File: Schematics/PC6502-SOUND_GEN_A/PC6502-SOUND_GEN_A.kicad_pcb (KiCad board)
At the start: 4 copper layers, 100 x 100 mm, 71 parts, among them IC1 AS7C164A-15PCN, IC2 AS7C164A-15PCN, IC3 AS7C164A-15PCN, IC4 AS7C164A-15PCN, IC5 AS7C164A-15PCN, IC6 AS7C164A-15PCN, J1 BUS, J2 NCO_OUT, J3 SND0/SND1, J5 Conn_02x05_Odd_Even, U1 74LS283, U10 74HCT574, U11 74HCT574, U12 74HC245, U13 74LS283, U14 74LS283, U15 74HCT574, U16 74HCT138, U2 74HC245, U3 74LS283, U4 ATF1502AS, U5 74HC245, U6 74AHCT244, U7 74HC14, U8 74LS283, U9 74LS283, X1 CXO_DIP8

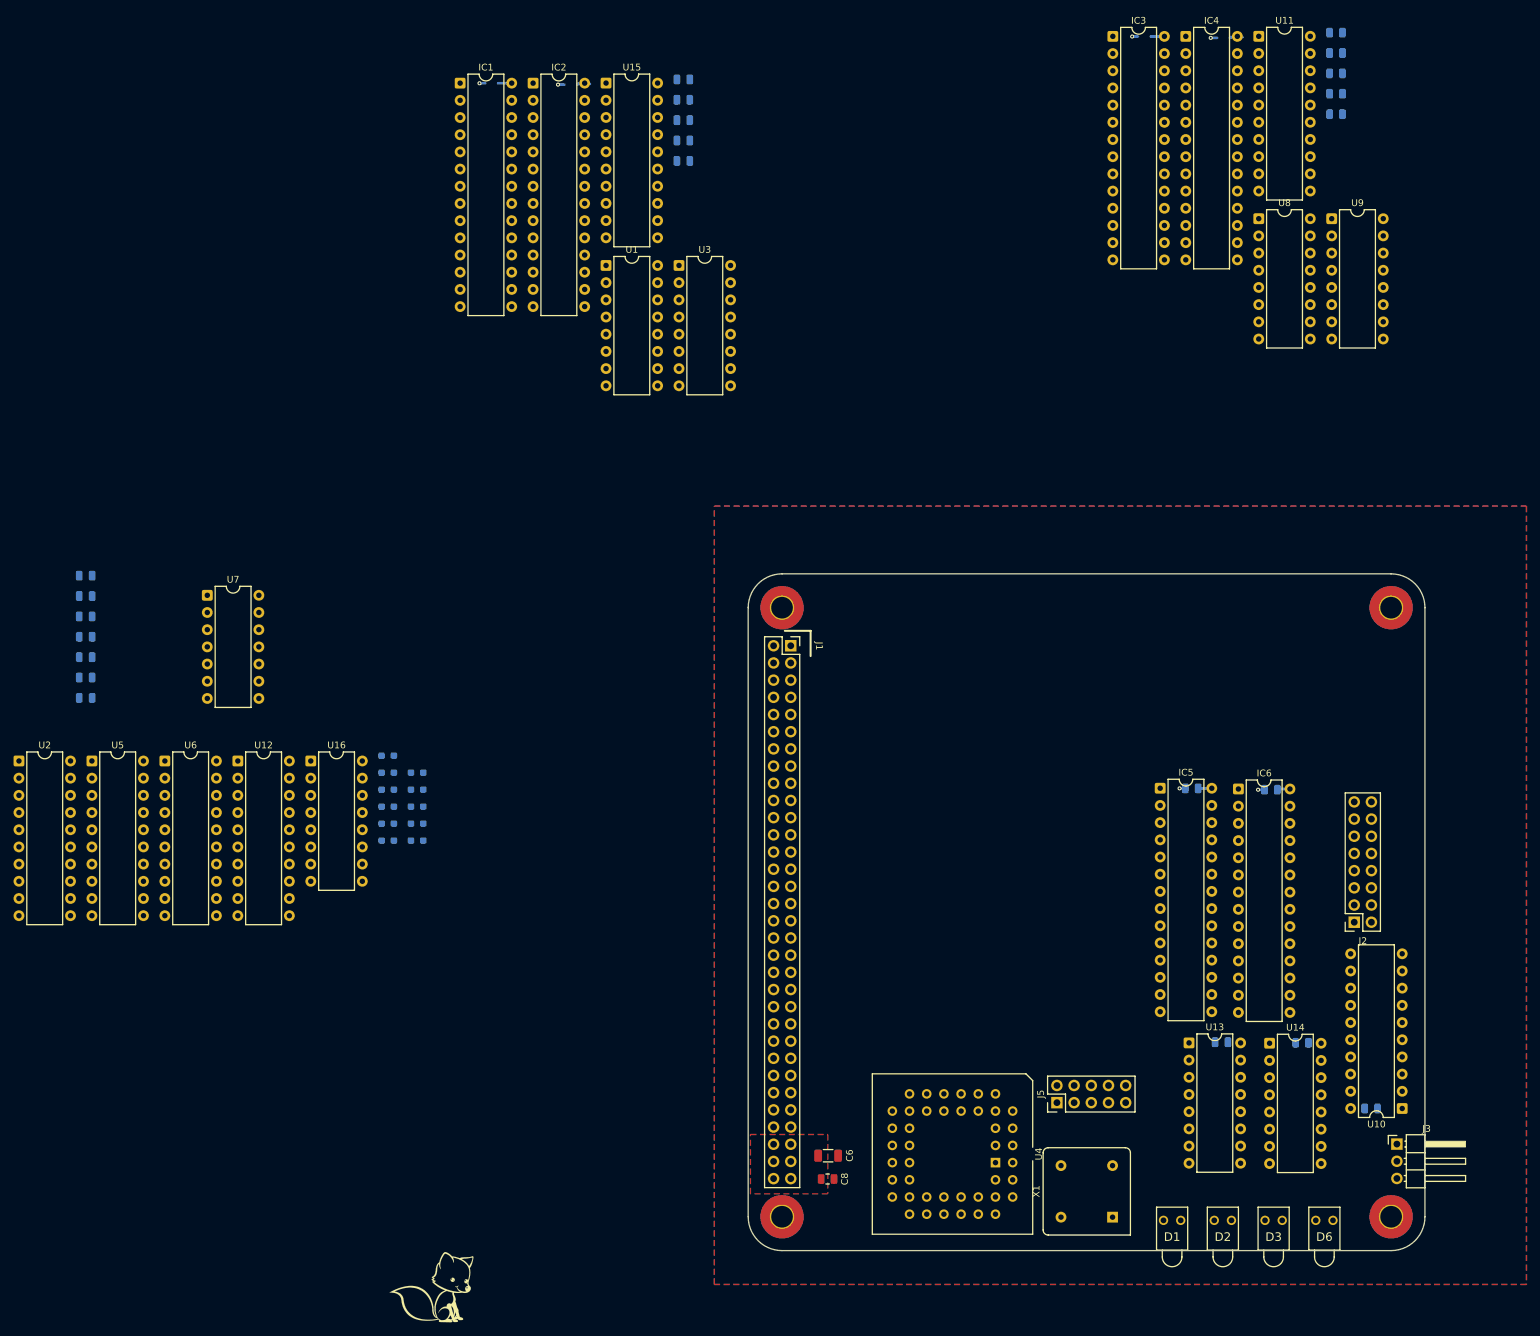
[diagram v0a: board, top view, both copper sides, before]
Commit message: Created V1.1 Schematic and PCB
A LOT of changes from v1.00;
removed clock stretcher (will now live in the CPLD)
moved the USB interface direct to the PCB
changed power pins
Added extra capacitance
Used Grant Searle's OSI basic and memory map to bring up the board
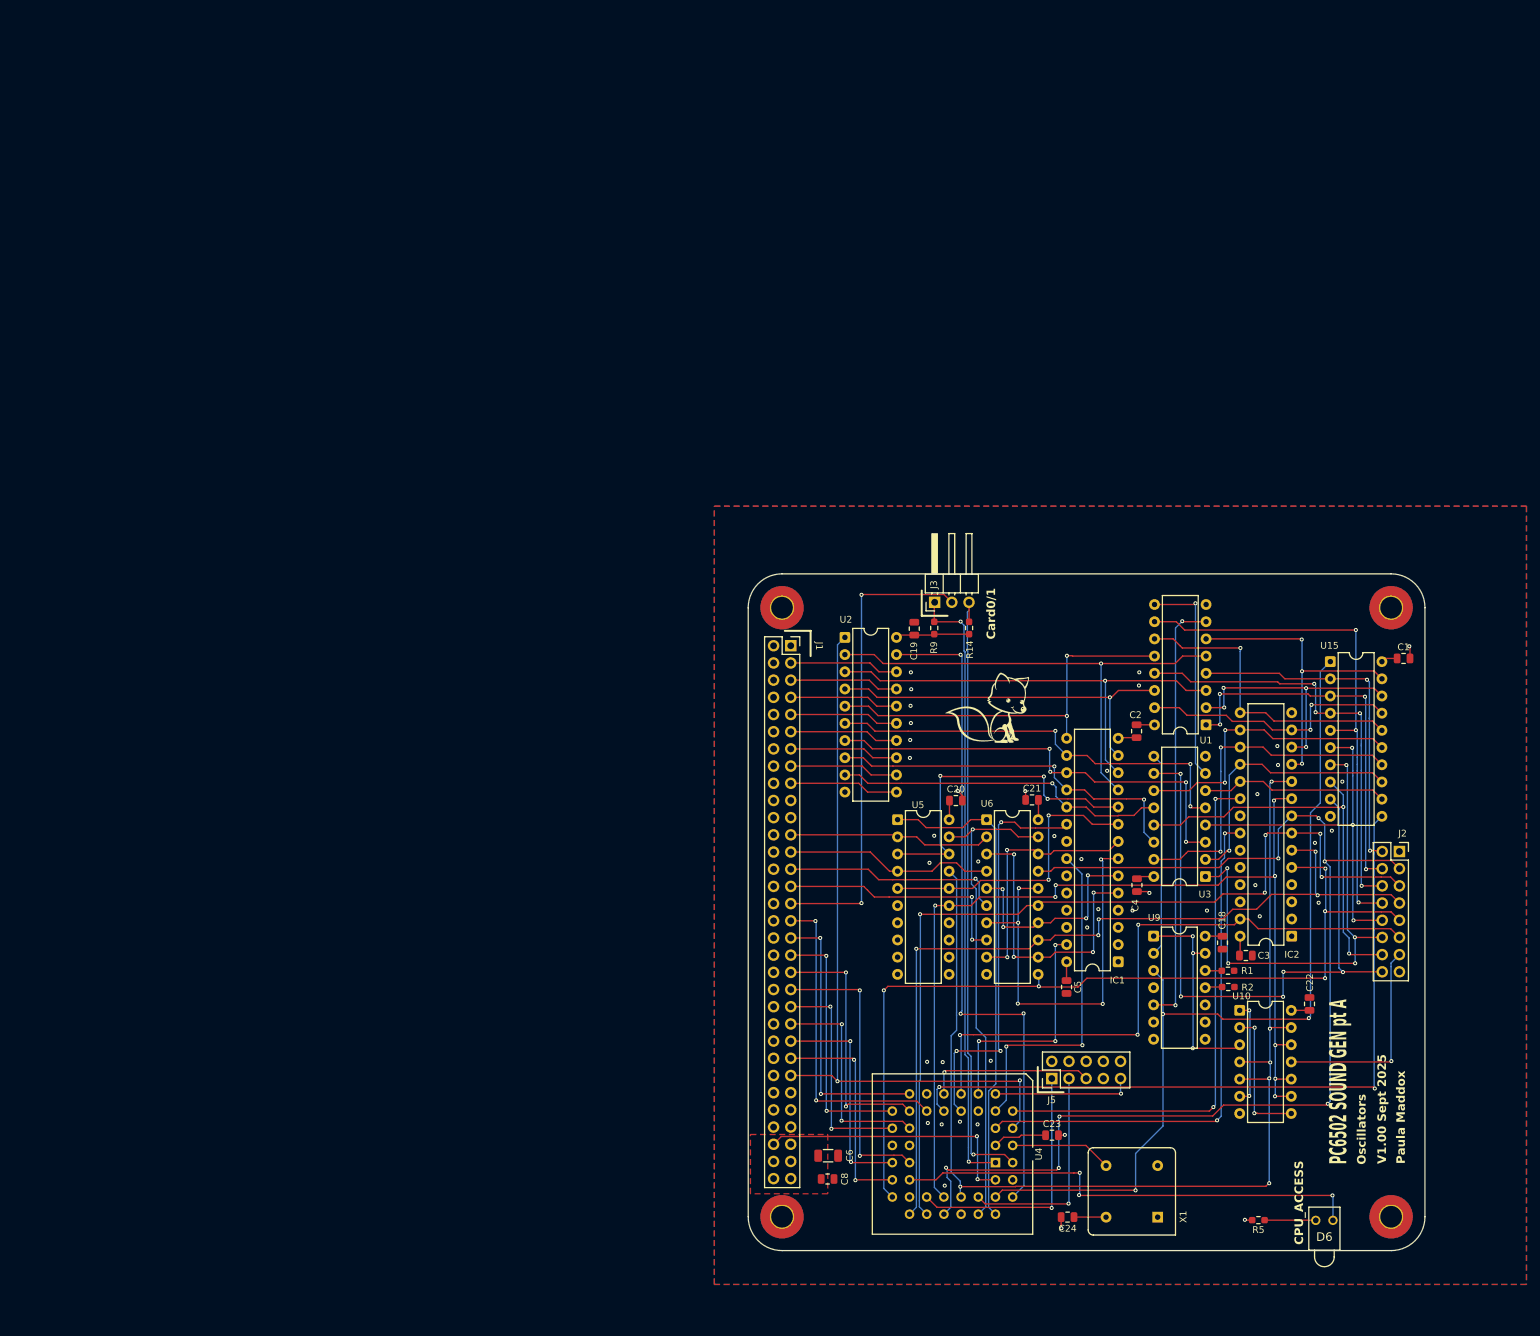
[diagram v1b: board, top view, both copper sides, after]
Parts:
- removed C10, C11, C12, C13, C14, C15, C16, C17, C7, C9: 100nF, Capacitor_SMD:C_0805_2012Metric
- removed D1, D2, D3: LED, LTL-4221NHBP:LTL4221NHBP
- removed IC3, IC4, IC5, IC6: AS7C164A-15PCN, Package_DIP:DIP-28_W7.62mm
- removed R10, R3, R4: 10K, Resistor_SMD:R_0603_1608Metric_Pad0.98x0.95mm_HandSolder
- removed R6, R7, R8: 470R, Resistor_SMD:R_0603_1608Metric_Pad0.98x0.95mm_HandSolder
- removed U11: 74HCT574, Package_DIP:DIP-20_W7.62mm
- removed U12: 74HC245, Package_DIP:DIP-20_W7.62mm
- removed U13, U14, U8: 74LS283, Package_DIP:DIP-16_W7.62mm
- removed U16: 74HCT138, Package_DIP:DIP-16_W7.62mm
- removed U7: 74HC14, Package_DIP:DIP-14_W7.62mm
- C1, C18, C19, C2, C20, C21, C22, C23, C24, C3, C4, C5, R1, R14, R2, R5, R9: moved to F.Cu
- U10: value 74HCT574 -> 74HC00; footprint Package_DIP:DIP-20_W7.62mm -> Package_DIP:DIP-14_W7.62mm
- U4: value ATF1502AS -> ATF1504AS
- U5: value 74HC245 -> 74AHCT244
- U9: value 74LS283 -> 74HC74; footprint Package_DIP:DIP-16_W7.62mm -> Package_DIP:DIP-14_W7.62mm
- moved C22 189.7 mm to (180.0, 108.5), turned to 90 degrees
- moved C24 173.3 mm to (144.2, 140.1), turned to 180 degrees
- moved C18 171.8 mm to (167.2, 99.5), turned to -90 degrees
- moved IC2 168.7 mm to (177.4, 98.5), turned to 180 degrees
- moved C23 163.5 mm to (141.9, 128.0)
- moved IC1 162.2 mm to (151.7, 102.3), turned to 180 degrees
- moved C3 148.8 mm to (170.6, 101.4)
- moved C5 145.6 mm to (144.1, 106.0), turned to -90 degrees
- moved R5 144.7 mm to (172.4, 140.5), turned to 180 degrees
- moved C21 141.9 mm to (139.0, 78.4), turned to 180 degrees
- moved U15 137.0 mm to (183.1, 58.0)
- moved C4 134.0 mm to (154.5, 91.0), turned to -90 degrees
- moved C20 130.3 mm to (127.8, 78.5)
- moved C1 129.4 mm to (193.9, 57.5)
- moved R2 126.5 mm to (168.0, 106.0)
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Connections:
- IC1 pad 10: OSC_A0 -> /8BitNCO/PTC_A0
- IC1 pad 20: PTC_LSB_nCS -> PTC_nCS
- IC1 pad 22: PTC_LSB_nOE -> PTC_nOE
- IC1 pad 27: PTC_LSB_nWR -> PTC_nWR
- IC1 pad 3: /8BitNCO/PTC_A7 -> GND
- IC1 pad 4: /8BitNCO/PTC_A6 -> GND
- IC1 pad 7: OSC_A3 -> /8BitNCO/PTC_A3
- IC1 pad 8: OSC_A2 -> /8BitNCO/PTC_A2
- IC1 pad 9: OSC_A1 -> /8BitNCO/PTC_A1
- IC2 pad 10: /ACC_AD_0 -> BYTE_SEL_A0
- IC2 pad 20: GND -> ACC_nCS
- IC2 pad 3: /8BitNCO/ACC_A7 -> GND
- IC2 pad 4: /8BitNCO/ACC_A6 -> GND
- IC2 pad 5: /8BitNCO/ACC_A5 -> OSC_A3
- IC2 pad 6: /8BitNCO/ACC_A4 -> OSC_A2
- IC2 pad 7: /ACC_AD_3 -> OSC_A1
- IC2 pad 8: /ACC_AD_2 -> OSC_A0
- IC2 pad 9: /ACC_AD_1 -> BYTE_SEL_A1
- J2 pad 10: /8BitNCO2/SUM4 -> /8BitNCO/SUM4
- J2 pad 12: /8BitNCO2/SUM5 -> /8BitNCO/SUM5
- J2 pad 13: SUB_BUF_nOE -> /nWAVE_VALID
- J2 pad 14: /8BitNCO2/SUM6 -> /8BitNCO/SUM6
- J2 pad 16: /8BitNCO2/SUM7 -> /8BitNCO/SUM7
- J2 pad 2: /8BitNCO2/SUM0 -> /8BitNCO/SUM0
- J2 pad 4: /8BitNCO2/SUM1 -> /8BitNCO/SUM1
- J2 pad 6: /8BitNCO2/SUM2 -> /8BitNCO/SUM2
- J2 pad 8: /8BitNCO2/SUM3 -> /8BitNCO/SUM3
- R1 pad 1: +5V -> Net-(U9B-D)
- R1 pad 2: Net-(U16-E2) -> GND
- R2 pad 1: +5V -> Net-(U9B-C)
- R2 pad 2: Net-(U16-~{Y0}) -> GND
- U1 pad 7: GND -> /8BitNCO/Cin
- U10 pad 1: SUB_BUF_nOE -> Net-(U10-Pad1)
- U10 pad 10: GND -> BYTE_SEL_A1
- U10 pad 11: SUM_BUF_CK -> /nWAVE_VALID
- U10 pad 12: /8BitNCO2/ACC_DQ7 -> BYTE_SEL_A1
- U10 pad 13: /8BitNCO2/ACC_DQ6 -> BYTE_SEL_A0
- U10 pad 14: /8BitNCO2/ACC_DQ5 -> +5V
- U10 pad 2: /8BitNCO2/SUM0 -> Net-(U10-Pad2)
- U10 pad 3: /8BitNCO2/SUM1 -> /nZERO_CARRY
- U10 pad 4: /8BitNCO2/SUM2 -> BYTE_SEL_A0
- U10 pad 5: /8BitNCO2/SUM3 -> BYTE_SEL_A0
- U10 pad 6: /8BitNCO2/SUM4 -> Net-(U10-Pad1)
- U10 pad 7: /8BitNCO2/SUM5 -> GND
- U10 pad 8: /8BitNCO2/SUM6 -> Net-(U10-Pad2)
- U10 pad 9: /8BitNCO2/SUM7 -> BYTE_SEL_A1
- U15 pad 1: SUB_BUF_nOE -> SUM_BUFF_nOE
- U15 pad 11: SUM_BUF_CK -> SUM_BUFF_CK
- U2 pad 1: +5V -> RnW
- U2 pad 11: /8BitNCO/PTC_DQ7 -> /D7
- U2 pad 12: /8BitNCO/PTC_DQ6 -> /D6
- U2 pad 13: /8BitNCO/PTC_DQ5 -> /D5
- U2 pad 14: /8BitNCO/PTC_DQ4 -> /D4
- U2 pad 15: /8BitNCO/PTC_DQ3 -> /D3
- U2 pad 16: /8BitNCO/PTC_DQ2 -> /D2
- U2 pad 17: /8BitNCO/PTC_DQ1 -> /D1
- U2 pad 18: /8BitNCO/PTC_DQ0 -> /D0
- U2 pad 19: Net-(U16-~{Y0}) -> nSYSDATA_TO_PTC
- U2 pad 2: /D0 -> /8BitNCO/PTC_DQ0
- U2 pad 3: /D1 -> /8BitNCO/PTC_DQ1
- U2 pad 4: /D2 -> /8BitNCO/PTC_DQ2
- U2 pad 5: /D3 -> /8BitNCO/PTC_DQ3
- U2 pad 6: /D4 -> /8BitNCO/PTC_DQ4
- U2 pad 7: /D5 -> /8BitNCO/PTC_DQ5
- U2 pad 8: /D6 -> /8BitNCO/PTC_DQ6
- U2 pad 9: /D7 -> /8BitNCO/PTC_DQ7
- U4 pad 11: SUB_BUF_nOE -> ACC_nWR
- U4 pad 12: PTC_MSB_nCS -> PTC_nCS
- U4 pad 14: PTC_HSB_nCS -> SUM_BUFF_CK
- U4 pad 34: SYS_DATA_nEN -> BYTE_SEL_A1
- U4 pad 36: NCO_ADDR_nEN -> BYTE_SEL_A0
- U4 pad 37: PTC_HSB_nWR -> NCO_ADDR_nEN
- U4 pad 39: PTC_LSB_nWR -> SYS_ADDR_nEN
- U4 pad 40: PTC_MSB_nWR -> nSYSDATA_TO_PTC
- U4 pad 41: SYS_ADDR_nEN -> SUM_BUFF_nOE
- U4 pad 5: SUM_BUF_CK -> ACC_nOE
- U4 pad 6: ACC_nOE -> ACC_nCS
- U4 pad 8: ACC_nWR -> PTC_nOE
- U4 pad 9: PTC_LSB_nCS -> PTC_nWR
- U5 pad 1: +5V -> SYS_ADDR_nEN
- U5 pad 11: /8BitNCO1/PTC_DQ7 -> GND
- U5 pad 12: /8BitNCO1/PTC_DQ6 -> unconnected-(U5-1Y3-Pad12)
- U5 pad 13: /8BitNCO1/PTC_DQ5 -> GND
- U5 pad 14: /8BitNCO1/PTC_DQ4 -> unconnected-(U5-1Y2-Pad14)
- U5 pad 15: /8BitNCO1/PTC_DQ3 -> BYTE_SEL_A1
- U5 pad 16: /8BitNCO1/PTC_DQ2 -> /8BitNCO/PTC_A1
- U5 pad 17: /8BitNCO1/PTC_DQ1 -> BYTE_SEL_A0
- U5 pad 18: /8BitNCO1/PTC_DQ0 -> /8BitNCO/PTC_A0
- U5 pad 19: Net-(U16-~{Y1}) -> NCO_ADDR_nEN
- U5 pad 2: /D0 -> /A2
- U5 pad 3: /D1 -> /8BitNCO/PTC_A0
- U5 pad 4: /D2 -> /A3
- U5 pad 5: /D3 -> /8BitNCO/PTC_A1
- U5 pad 6: /D4 -> GND
- U5 pad 7: /D5 -> unconnected-(U5-2Y2-Pad7)
- U5 pad 8: /D6 -> GND
- U5 pad 9: /D7 -> unconnected-(U5-2Y3-Pad9)
- U6 pad 12: /ACC_AD_3 -> /8BitNCO/PTC_A5
- U6 pad 14: /ACC_AD_2 -> /8BitNCO/PTC_A4
- U6 pad 16: /ACC_AD_1 -> /8BitNCO/PTC_A3
- U6 pad 18: /ACC_AD_0 -> /8BitNCO/PTC_A2
- U6 pad 2: /A0 -> /A2
- U6 pad 3: /ACC_AD_3 -> /8BitNCO/PTC_A5
- U6 pad 4: /A1 -> /A3
- U6 pad 5: /ACC_AD_2 -> /8BitNCO/PTC_A4
- U6 pad 6: /A2 -> /A4
- U6 pad 7: /ACC_AD_1 -> /8BitNCO/PTC_A3
- U6 pad 8: /A3 -> /A5
- U6 pad 9: /ACC_AD_0 -> /8BitNCO/PTC_A2
- U9 pad 1: /8BitNCO1/SUM5 -> /nZERO_CARRY
- U9 pad 10: /8BitNCO1/SUM7 -> +5V
- U9 pad 11: /8BitNCO1/ACC_DQ4 -> Net-(U9B-C)
- U9 pad 12: /8BitNCO1/PTC_DQ7 -> Net-(U9B-D)
- U9 pad 13: /8BitNCO1/SUM6 -> /nZERO_CARRY
- U9 pad 14: /8BitNCO1/PTC_DQ6 -> +5V
- U9 pad 2: /8BitNCO1/ACC_DQ6 -> /8BitNCO/Cout
- U9 pad 3: /8BitNCO1/PTC_DQ5 -> SUM_BUFF_nOE
- U9 pad 4: /8BitNCO1/SUM4 -> +5V
- U9 pad 5: /8BitNCO1/PTC_DQ4 -> /8BitNCO/Cin
- U9 pad 6: /8BitNCO1/ACC_DQ7 -> unconnected-(U9A-~{Q}-Pad6)
- U9 pad 7: Net-(U8-C4) -> GND
- U9 pad 8: GND -> unconnected-(U9B-~{Q}-Pad8)
- U9 pad 9: /8BitNCO1/Cout -> unconnected-(U9B-Q-Pad9)
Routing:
- net OSC_A0: track 0.00 -> 174.7 mm, vias 0 -> 7
- net BYTE_SEL_A0: track 0.00 -> 170.1 mm, vias 0 -> 6
- net BYTE_SEL_A1: track 0.00 -> 150.4 mm, vias 0 -> 8
- net OSC_A1: track 0.00 -> 132.5 mm, vias 0 -> 5
- net SUM_BUFF_nOE: track 0.00 -> 131.8 mm, vias 0 -> 3
- net OSC_A3: track 0.00 -> 131.7 mm, vias 0 -> 5
- net OSC_A2: track 0.00 -> 126.5 mm, vias 0 -> 5
- net SUM_BUFF_CK: track 0.00 -> 109.3 mm, vias 0 -> 2
- net RnW: track 0.00 -> 107.8 mm, vias 0 -> 2
- net nSYSDATA_TO_PTC: track 0.00 -> 100.0 mm, vias 0 -> 3
- net /8BitNCO/SUM7: track 0.00 -> 96.7 mm, vias 0 -> 5
- net ACC_nWR: track 0.00 -> 91.4 mm, vias 0 -> 3
- net Net-(J3-Pin_3): track 0.00 -> 91.4 mm, vias 0 -> 1
- net Net-(J3-Pin_1): track 0.00 -> 91.1 mm, vias 0 -> 2
- net ACC_nCS: track 0.00 -> 79.2 mm, vias 0 -> 2
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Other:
- board text added: "CPU_ACCESS"
- board text added: "Card0/1"
- board text added: "Oscillators"
- board text added: "PC6502 SOUND GEN pt A"
- board text added: "Paula Maddox"
- board text added: "V1.00 Sept 2025"

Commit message: Update KeyTFT CPLD
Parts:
- removed R14, R9: 10K, Resistor_SMD:R_0603_1608Metric_Pad0.98x0.95mm_HandSolder
- added J4: Conn_01x09, Connector_PinSocket_2.54mm:PinSocket_1x09_P2.54mm_Vertical, F.Cu at (194.1, 58.0)
- moved C1 4.73 mm to (189.8, 55.2), turned to 180 degrees
- moved J5 0.82 mm to (142.7, 119.6)
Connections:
- net CLK renamed SYSCLK
- net nSLOW renamed nSLOW0
- J1 pad 12: GND -> +5V
- J1 pad 16: GND -> +5V
- J1 pad 20: GND -> +5V
- J1 pad 24: GND -> +5V
- J1 pad 28: GND -> +5V
- J1 pad 32: GND -> +5V
- J1 pad 36: GND -> +5V
- J1 pad 4: GND -> +5V
- J1 pad 40: GND -> +5V
- J1 pad 44: GND -> +5V
- J1 pad 48: GND -> +5V
- J1 pad 55: nBUSRQ -> nSLOW1
- J1 pad 57: nRES -> RDY
- J1 pad 59: +5V -> nVP
- J1 pad 61: +5V -> nBUSRQ
- J1 pad 62: +5V -> unconnected-(J1-Pin_62-Pad62)
- J1 pad 63: +5V -> nRES
- J1 pad 64: +5V -> GND
- J1 pad 8: GND -> +5V
- J3 pad 1: Net-(J3-Pin_1) -> +5V
- J3 pad 2: /A6 -> Net-(J3-Pin_2)
- J3 pad 3: Net-(J3-Pin_3) -> GND
- U4 pad 1: Net-(J3-Pin_1) -> Net-(J3-Pin_2)
- U4 pad 11: ACC_nWR -> unconnected-(U4-I/O/PD1-Pad11)
- U4 pad 4: RnW -> ACC_nWR
- U4 pad 43: CPU_CLK -> RnW
- U4 pad 44: Net-(J3-Pin_3) -> /A6
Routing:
- net Net-(J3-Pin_3): track 91.4 -> 0.00 mm, vias 1 -> 0
- net Net-(J3-Pin_1): track 91.1 -> 0.00 mm, vias 2 -> 0
- net Net-(J3-Pin_2): track 0.00 -> 88.0 mm, vias 0 -> 1
- net CPU_CLK: track 39.6 -> 0.00 mm, vias 2 -> 0
- net GND: track 12.2 -> 18.1 mm, vias 41 -> 45
- net RnW: track 107.8 -> 111.4 mm, vias 2 -> 3
- net /8BitNCO/ACC_DQ5: track 50.7 -> 54.1 mm
- net /8BitNCO/ACC_DQ3: track 44.9 -> 48.2 mm
- net /8BitNCO/ACC_DQ0: track 46.4 -> 49.8 mm
- net /8BitNCO/ACC_DQ7: track 27.7 -> 31.1 mm
- net /8BitNCO/ACC_DQ4: track 43.0 -> 46.4 mm
- net /8BitNCO/ACC_DQ2: track 39.1 -> 42.5 mm
- net /8BitNCO/ACC_DQ1: track 40.4 -> 43.7 mm
- net /8BitNCO/ACC_DQ6: track 39.5 -> 42.9 mm
- net ACC_nWR: track 91.4 -> 88.0 mm
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- removed copper zone on F.Cu, net +5V
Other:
- board text added: "74HC00"
- board text added: "74HC244"
- board text added: "74HC245"
- board text added: "74HC74"
- board text added: "74LS283"
- board text added: "AS7C164A-15PCN"
